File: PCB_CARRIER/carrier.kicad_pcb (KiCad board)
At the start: 6 copper layers, 69.6 x 46.1 mm, 98 parts, among them J1 SODIMM-260_Split, J2 Micro_SD_Card_Det2, Q2 BSS138, Q3 BSS138, Q4 BC817-40, Q5 BSS138, SW1 SW_DIP_x04, U1 SN74LVC8T245, U2 SN74LVC8T245, U3 SN74LVC8T245, U4 RT9742GGJ5

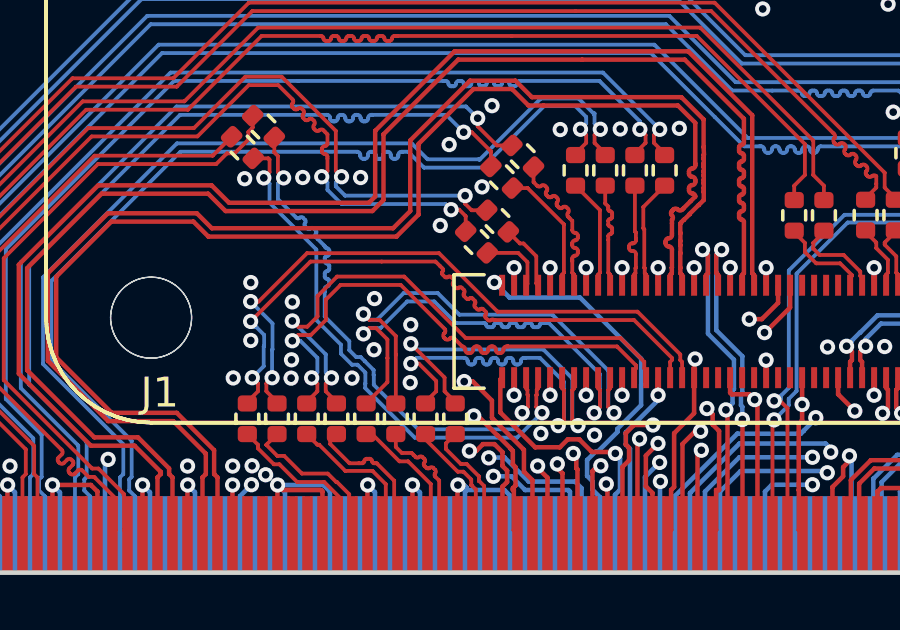
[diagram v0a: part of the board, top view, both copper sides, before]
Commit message: fixing an EMI problem!
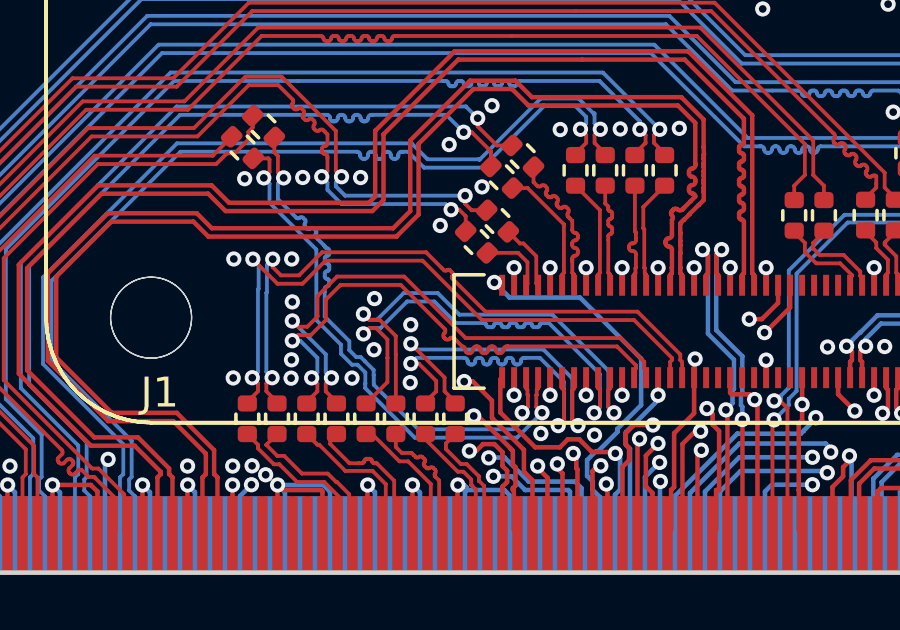
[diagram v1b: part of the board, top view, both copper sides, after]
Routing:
- net HDMI-0_TX2_N: track 21.1 -> 21.9 mm
- net HDMI-0_TX2_P: track 21.1 -> 21.8 mm
